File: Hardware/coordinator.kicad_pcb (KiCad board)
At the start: 4 copper layers, 140 x 140 mm, 111 parts, among them CON1 Nucleo-144-zio, CON10 Home Sensor, CON11 Home Sensor, CON12 Home Sensor, CON13 Home Sensor, CON14 Emergency Stop, CON15 Expansion, CON16 +24V Power in, CON2 DB25 Main Motor Signal, CON3 DB25 Main Motor Signal, CON4 DB25 Main Motor Signal, CON5 DB25 Main Motor Signal, CON6 DB25 Main Motor Signal, CON7 DB25 Main Motor Signal, CON8 Home Sensor, CON9 Home Sensor, J1 E5V, J2 PA1, U1 AM26LV32xD, U10 TLP293-4, U11 TLP293-4, U12 TLP293-4, U13 TLP293-4, U14 TLP293-4, U15 TLP293-4, U16 PDQE10, U2 AM26LV32xD, U3 AM26LV32xD, U4 DS26LV31T, U5 DS26LV31T, U6 DS26LV31T, U7 TLP293-4, U8 TLP293-4, U9 TLP293-4

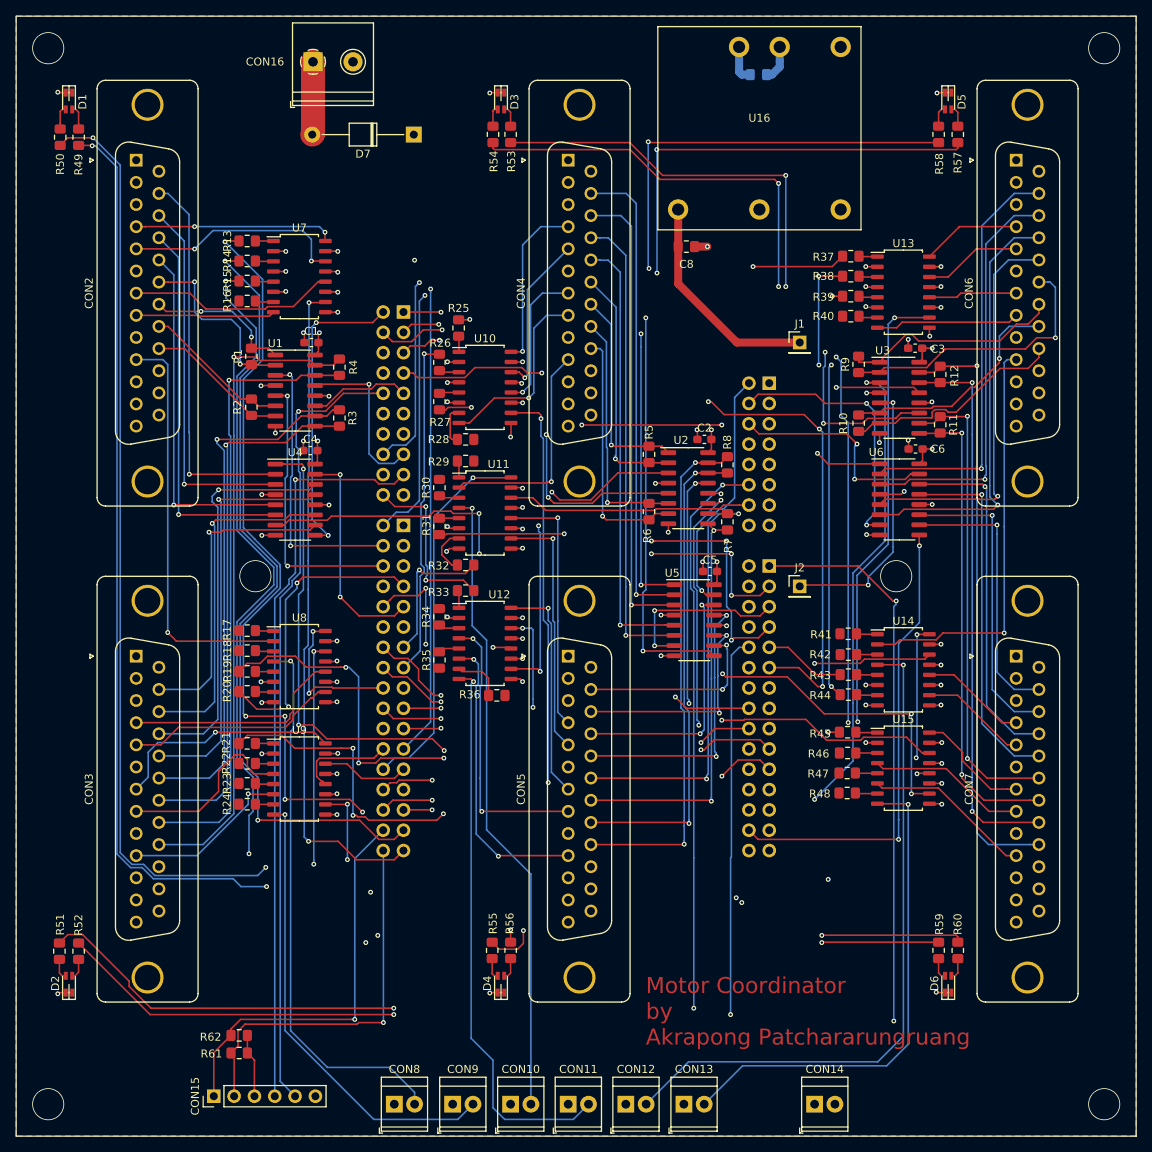
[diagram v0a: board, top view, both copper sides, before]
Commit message: Original commit of version 2. The firmware is similar to version 1 plus some bug fixes
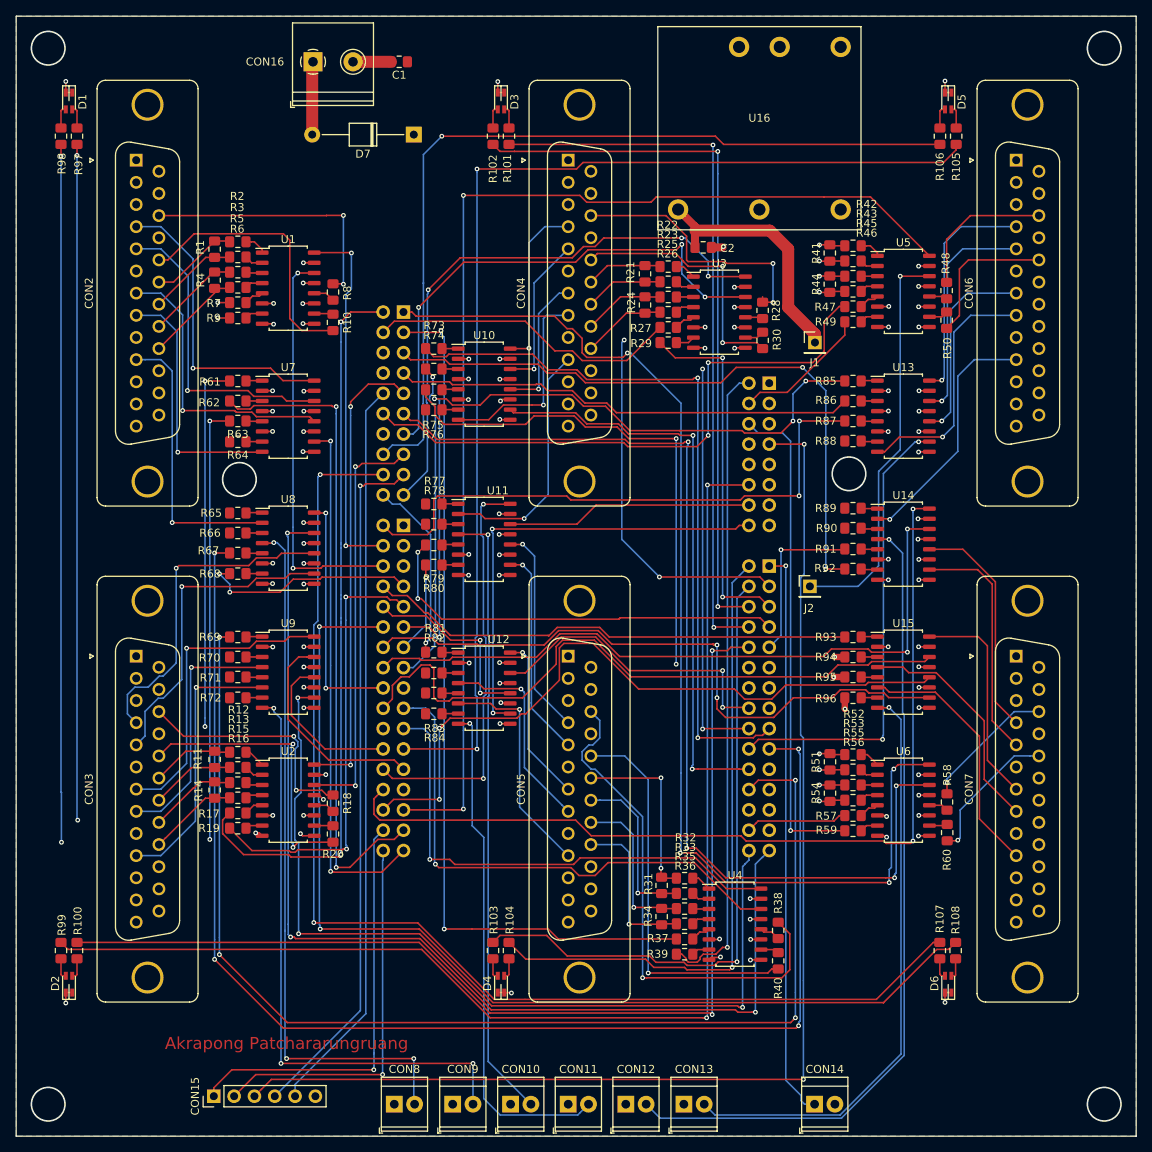
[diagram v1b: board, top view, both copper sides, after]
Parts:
- removed C3, C4, C5, C6: 0.1uF, Capacitor_SMD:C_0603_1608Metric_Pad1.05x0.95mm_HandSolder
- removed C7, C8: 10uF 25V, Capacitor_SMD:C_0805_2012Metric_Pad1.15x1.40mm_HandSolder
- added R100: 330, Resistor_SMD:R_0805_2012Metric_Pad1.15x1.40mm_HandSolder, F.Cu at (87.6, 136.8)
- added R101: 330, Resistor_SMD:R_0805_2012Metric_Pad1.15x1.40mm_HandSolder, F.Cu at (141.6, 35.0)
- added R102: 330, Resistor_SMD:R_0805_2012Metric_Pad1.15x1.40mm_HandSolder, F.Cu at (139.6, 35.0)
- added R103: 330, Resistor_SMD:R_0805_2012Metric_Pad1.15x1.40mm_HandSolder, F.Cu at (139.6, 136.8)
- added R104: 330, Resistor_SMD:R_0805_2012Metric_Pad1.15x1.40mm_HandSolder, F.Cu at (141.6, 136.8)
- added R105: 330, Resistor_SMD:R_0805_2012Metric_Pad1.15x1.40mm_HandSolder, F.Cu at (197.5, 35.0)
- added R106: 330, Resistor_SMD:R_0805_2012Metric_Pad1.15x1.40mm_HandSolder, F.Cu at (195.5, 35.0)
- added R107: 330, Resistor_SMD:R_0805_2012Metric_Pad1.15x1.40mm_HandSolder, F.Cu at (195.4, 136.8)
- added R108: 330, Resistor_SMD:R_0805_2012Metric_Pad1.15x1.40mm_HandSolder, F.Cu at (197.4, 136.8)
- added R63: 330, Resistor_SMD:R_0805_2012Metric_Pad1.15x1.40mm_HandSolder, F.Cu at (107.7, 70.6)
- added R64: 4.7K, Resistor_SMD:R_0805_2012Metric_Pad1.15x1.40mm_HandSolder, F.Cu at (107.7, 73.2)
- added R65: 4.7K, Resistor_SMD:R_0805_2012Metric_Pad1.15x1.40mm_HandSolder, F.Cu at (107.7, 82.1)
- added R66: 4.7K, Resistor_SMD:R_0805_2012Metric_Pad1.15x1.40mm_HandSolder, F.Cu at (107.7, 84.6)
- added R67: 330, Resistor_SMD:R_0805_2012Metric_Pad1.15x1.40mm_HandSolder, F.Cu at (107.7, 87.1)
- added R68: 330, Resistor_SMD:R_0805_2012Metric_Pad1.15x1.40mm_HandSolder, F.Cu at (107.7, 89.7)
- added R69: 330, Resistor_SMD:R_0805_2012Metric_Pad1.15x1.40mm_HandSolder, F.Cu at (107.7, 97.6)
- added R70: 4.7K, Resistor_SMD:R_0805_2012Metric_Pad1.15x1.40mm_HandSolder, F.Cu at (107.7, 100.1)
- added R71: 4.7K, Resistor_SMD:R_0805_2012Metric_Pad1.15x1.40mm_HandSolder, F.Cu at (107.7, 102.6)
- added R72: 4.7K, Resistor_SMD:R_0805_2012Metric_Pad1.15x1.40mm_HandSolder, F.Cu at (107.7, 105.2)
- added R73: 330, Resistor_SMD:R_0805_2012Metric_Pad1.15x1.40mm_HandSolder, F.Cu at (132.2, 61.5)
- added R74: 330, Resistor_SMD:R_0805_2012Metric_Pad1.15x1.40mm_HandSolder, F.Cu at (132.2, 64.1)
- added R75: 330, Resistor_SMD:R_0805_2012Metric_Pad1.15x1.40mm_HandSolder, F.Cu at (132.2, 66.7)
- added R76: 4.7K, Resistor_SMD:R_0805_2012Metric_Pad1.15x1.40mm_HandSolder, F.Cu at (132.2, 69.2)
- added R77: 4.7K, Resistor_SMD:R_0805_2012Metric_Pad1.15x1.40mm_HandSolder, F.Cu at (132.2, 81.0)
- added R78: 4.7K, Resistor_SMD:R_0805_2012Metric_Pad1.15x1.40mm_HandSolder, F.Cu at (132.2, 83.5)
- added R79: 330, Resistor_SMD:R_0805_2012Metric_Pad1.15x1.40mm_HandSolder, F.Cu at (132.2, 86.1)
- added R80: 330, Resistor_SMD:R_0805_2012Metric_Pad1.15x1.40mm_HandSolder, F.Cu at (132.2, 88.6)
- added R81: 330, Resistor_SMD:R_0805_2012Metric_Pad1.15x1.40mm_HandSolder, F.Cu at (132.2, 99.5)
- added R82: 4.7K, Resistor_SMD:R_0805_2012Metric_Pad1.15x1.40mm_HandSolder, F.Cu at (132.2, 102.1)
- added R83: 4.7K, Resistor_SMD:R_0805_2012Metric_Pad1.15x1.40mm_HandSolder, F.Cu at (132.2, 104.6)
- added R84: 4.7K, Resistor_SMD:R_0805_2012Metric_Pad1.15x1.40mm_HandSolder, F.Cu at (132.2, 107.2)
- added R85: 330, Resistor_SMD:R_0805_2012Metric_Pad1.15x1.40mm_HandSolder, F.Cu at (184.6, 65.6)
- added R86: 330, Resistor_SMD:R_0805_2012Metric_Pad1.15x1.40mm_HandSolder, F.Cu at (184.6, 68.1)
- added R87: 330, Resistor_SMD:R_0805_2012Metric_Pad1.15x1.40mm_HandSolder, F.Cu at (184.6, 70.6)
- added R88: 4.7K, Resistor_SMD:R_0805_2012Metric_Pad1.15x1.40mm_HandSolder, F.Cu at (184.6, 73.1)
- added R89: 4.7K, Resistor_SMD:R_0805_2012Metric_Pad1.15x1.40mm_HandSolder, F.Cu at (184.6, 81.5)
- added R90: 4.7K, Resistor_SMD:R_0805_2012Metric_Pad1.15x1.40mm_HandSolder, F.Cu at (184.6, 84.0)
- added R91: 330, Resistor_SMD:R_0805_2012Metric_Pad1.15x1.40mm_HandSolder, F.Cu at (184.6, 86.6)
- added R92: 330, Resistor_SMD:R_0805_2012Metric_Pad1.15x1.40mm_HandSolder, F.Cu at (184.6, 89.1)
- added R93: 330, Resistor_SMD:R_0805_2012Metric_Pad1.15x1.40mm_HandSolder, F.Cu at (184.6, 97.6)
- added R94: 4.7K, Resistor_SMD:R_0805_2012Metric_Pad1.15x1.40mm_HandSolder, F.Cu at (184.6, 100.1)
- added R95: 4.7K, Resistor_SMD:R_0805_2012Metric_Pad1.15x1.40mm_HandSolder, F.Cu at (184.6, 102.6)
- added R96: 4.7K, Resistor_SMD:R_0805_2012Metric_Pad1.15x1.40mm_HandSolder, F.Cu at (184.6, 105.2)
- added R97: 330, Resistor_SMD:R_0805_2012Metric_Pad1.15x1.40mm_HandSolder, F.Cu at (87.6, 35.0)
- added R98: 330, Resistor_SMD:R_0805_2012Metric_Pad1.15x1.40mm_HandSolder, F.Cu at (85.6, 35.0)
- added R99: 330, Resistor_SMD:R_0805_2012Metric_Pad1.15x1.40mm_HandSolder, F.Cu at (85.6, 136.8)
- C1, C2: value 0.1uF -> 10uF 25V; footprint Capacitor_SMD:C_0603_1608Metric_Pad1.05x0.95mm_HandSolder -> Capacitor_SMD:C_0805_2012Metric_Pad1.15x1.40mm_HandSolder
- R1, R11: value 120 -> 680
- R10, R8: value 120 -> 3.6k
- R12, R2, R3, R5, R6, R7, R9: value 120 -> 330
- R14, R44, R54: value 330 -> 120
- R16, R17, R22, R23, R29, R35, R36, R42, R46, R47, R61, R62: value 4.7K -> 330
- R18, R28, R30, R40, R48: value 4.7K -> 3.6k
- R20, R38, R50, R58, R60: value 330 -> 3.6k
- R21, R31, R51: value 330 -> 680
- R24, R34: value 4.7K -> 120
- R41: value 4.7K -> 680
- U1, U2, U3: value AM26LV32xD -> TLP292-4; footprint Package_SO:SOIC-16_3.9x9.9mm_P1.27mm -> Package_SO:SOIC-16_4.55x10.3mm_P1.27mm
- U10, U11, U12, U13, U14, U15, U7, U8, U9: value TLP293-4 -> TLP292-4
- U4, U5, U6: value DS26LV31T -> TLP292-4; footprint Package_SO:SOIC-16_3.9x9.9mm_P1.27mm -> Package_SO:SOIC-16_4.55x10.3mm_P1.27mm
- moved R50 113.1 mm to (196.3, 58.0), turned to 270 degrees
- moved R11 99.9 mm to (104.8, 112.9)
- moved R52 99.9 mm to (184.6, 112.3), turned to 0 degrees
- moved R12 99.7 mm to (107.7, 112.0), turned to 0 degrees
- moved R49 99.5 mm to (184.6, 58.2), turned to 0 degrees
- moved R51 99.2 mm to (181.7, 113.2)
- moved R54 92.5 mm to (181.7, 117.1), turned to 270 degrees
- moved R53 90.2 mm to (184.6, 114.2), turned to 0 degrees
- moved R37 87.8 mm to (163.6, 135.3), turned to 0 degrees
- moved R57 86.2 mm to (184.6, 119.9), turned to 0 degrees
- moved R39 84.8 mm to (163.6, 137.2), turned to 0 degrees
- moved R61 84.0 mm to (107.7, 65.6)
- moved R58 83.5 mm to (196.3, 118.2)
- moved R38 82.3 mm to (175.2, 134.3), turned to 90 degrees
- moved R23 81.9 mm to (161.5, 53.2), turned to 0 degrees
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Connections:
- C1 pad 1: GND -> +24V
- C1 pad 2: +3V3 -> GNDPWR
- C2 pad 1: GND -> +5V
- C2 pad 2: +3V3 -> GND
- CON2 pad 15: M1_PULSE_P -> +24V
- CON2 pad 17: M1_DIR_P -> +24V
- CON3 pad 15: M2_PULSE_P -> +24V
- CON3 pad 17: M2_DIR_P -> +24V
- CON4 pad 15: M3_PULSE_P -> +24V
- CON4 pad 17: M3_DIR_P -> +24V
- CON5 pad 15: M4_PULSE_P -> +24V
- CON5 pad 17: M4_DIR_P -> +24V
- CON6 pad 15: M5_PULSE_P -> +24V
- CON6 pad 17: M5_DIR_P -> +24V
- CON7 pad 15: M6_PULSE_P -> +24V
- CON7 pad 17: M6_DIR_P -> +24V
- R10 pad 1: M5_OUTB_P -> Net-(R10-Pad1)
- R10 pad 2: M5_OUTB_N -> M1_DIR_N
- R11 pad 1: M6_OUTA_P -> M2_OUTA_P
- R11 pad 2: M6_OUTA_N -> M2_OUTA_N
- R12 pad 1: M6_OUTB_P -> M2_OUTA_P
- R12 pad 2: M6_OUTB_N -> Net-(R12-Pad2)
- R13 pad 1: Net-(R13-Pad1) -> M2_OUTA_N
- R13 pad 2: M1_SRV_ON -> Net-(R13-Pad2)
- R14 pad 1: Net-(R14-Pad1) -> M2_OUTB_P
- R14 pad 2: M1_ALRM_RES -> M2_OUTB_N
- R15 pad 1: Net-(R15-Pad1) -> M2_OUTB_P
- R15 pad 2: M1_DEV_CLR -> Net-(R15-Pad2)
- R16 pad 1: Net-(R16-Pad1) -> M2_OUTB_N
- R16 pad 2: +24V -> Net-(R16-Pad2)
- R17 pad 1: Net-(R17-Pad1) -> M2_PULSE
- R17 pad 2: +24V -> Net-(R17-Pad2)
- R18 pad 2: +24V -> M2_PULSE_N
- R19 pad 1: Net-(R19-Pad1) -> M2_DIR
- R19 pad 2: M2_SRV_ON -> Net-(R19-Pad2)
- R2 pad 1: M1_OUTB_P -> M1_OUTA_P
- R2 pad 2: M1_OUTB_N -> Net-(R2-Pad2)
- R20 pad 2: M2_ALRM_RES -> M2_DIR_N
- R21 pad 1: Net-(R21-Pad1) -> M3_OUTA_P
- R21 pad 2: M2_DEV_CLR -> M3_OUTA_N
- R22 pad 1: Net-(R22-Pad1) -> M3_OUTA_P
- R22 pad 2: +24V -> Net-(R22-Pad2)
- R23 pad 1: Net-(R23-Pad1) -> M3_OUTA_N
- R23 pad 2: +24V -> Net-(R23-Pad2)
- R24 pad 1: Net-(R24-Pad1) -> M3_OUTB_P
- R24 pad 2: +24V -> M3_OUTB_N
- R25 pad 1: Net-(R25-Pad1) -> M3_OUTB_P
- R25 pad 2: M3_SRV_ON -> Net-(R25-Pad2)
- R26 pad 1: Net-(R26-Pad1) -> M3_OUTB_N
- R26 pad 2: M3_ALRM_RES -> Net-(R26-Pad2)
- R27 pad 1: Net-(R27-Pad1) -> M3_PULSE
- R27 pad 2: M3_DEV_CLR -> Net-(R27-Pad2)
- R28 pad 2: +24V -> M3_PULSE_N
- R29 pad 1: Net-(R29-Pad1) -> M3_DIR
- R29 pad 2: +24V -> Net-(R29-Pad2)
- R3 pad 1: M2_OUTA_P -> M1_OUTA_N
- R3 pad 2: M2_OUTA_N -> Net-(R3-Pad2)
- R30 pad 2: +24V -> M3_DIR_N
- R31 pad 1: Net-(R31-Pad1) -> M4_OUTA_P
- R31 pad 2: M4_SRV_ON -> M4_OUTA_N
- R32 pad 1: Net-(R32-Pad1) -> M4_OUTA_P
- R32 pad 2: M4_ALRM_RES -> Net-(R32-Pad2)
- R33 pad 1: Net-(R33-Pad1) -> M4_OUTA_N
- R33 pad 2: M4_DEV_CLR -> Net-(R33-Pad2)
- R34 pad 1: Net-(R34-Pad1) -> M4_OUTB_P
- R34 pad 2: +24V -> M4_OUTB_N
- R35 pad 1: Net-(R35-Pad1) -> M4_OUTB_P
- R35 pad 2: +24V -> Net-(R35-Pad2)
- R36 pad 1: Net-(R36-Pad1) -> M4_OUTB_N
- R36 pad 2: +24V -> Net-(R36-Pad2)
- R37 pad 1: Net-(R37-Pad1) -> M4_PULSE
- R37 pad 2: M5_SRV_ON -> Net-(R37-Pad2)
- R38 pad 2: M5_ALRM_RES -> M4_PULSE_N
- R39 pad 1: Net-(R39-Pad1) -> M4_DIR
- R39 pad 2: M5_DEV_CLR -> Net-(R39-Pad2)
- R4 pad 1: M2_OUTB_P -> M1_OUTB_P
- R4 pad 2: M2_OUTB_N -> M1_OUTB_N
- R40 pad 2: +24V -> M4_DIR_N
- R41 pad 1: Net-(R41-Pad1) -> M5_OUTA_P
- R41 pad 2: +24V -> M5_OUTA_N
- R42 pad 1: Net-(R42-Pad1) -> M5_OUTA_P
- R42 pad 2: +24V -> Net-(R42-Pad2)
- R43 pad 1: Net-(R43-Pad1) -> M5_OUTA_N
- R43 pad 2: M6_SRV_ON -> Net-(R43-Pad2)
- R44 pad 1: Net-(R44-Pad1) -> M5_OUTB_P
- R44 pad 2: M6_ALRM_RES -> M5_OUTB_N
- R45 pad 1: Net-(R45-Pad1) -> M5_OUTB_P
- R45 pad 2: M6_DEV_CLR -> Net-(R45-Pad2)
- R46 pad 1: Net-(R46-Pad1) -> M5_OUTB_N
- R46 pad 2: +24V -> Net-(R46-Pad2)
- R47 pad 1: Net-(R47-Pad1) -> M5_PULSE
- R47 pad 2: +24V -> Net-(R47-Pad2)
- R48 pad 2: +24V -> M5_PULSE_N
- R49 pad 1: Net-(CON1-Pad9-25) -> M5_DIR
- R49 pad 2: Net-(D1-Pad2) -> Net-(R49-Pad2)
- R5 pad 1: M3_OUTA_P -> M1_OUTB_P
- R5 pad 2: M3_OUTA_N -> Net-(R5-Pad2)
- R50 pad 1: Net-(CON1-Pad9-27) -> Net-(R50-Pad1)
- R50 pad 2: Net-(D1-Pad4) -> M5_DIR_N
- R51 pad 1: Net-(CON1-Pad8-12) -> M6_OUTA_P
- R51 pad 2: Net-(D2-Pad2) -> M6_OUTA_N
- R52 pad 1: Net-(CON1-Pad9-10) -> M6_OUTA_P
- R52 pad 2: Net-(D2-Pad4) -> Net-(R52-Pad2)
- R53 pad 1: Net-(CON1-Pad9-8) -> M6_OUTA_N
- R53 pad 2: Net-(D3-Pad2) -> Net-(R53-Pad2)
- R54 pad 1: Net-(CON1-Pad9-6) -> M6_OUTB_P
- R54 pad 2: Net-(D3-Pad4) -> M6_OUTB_N
- R55 pad 1: Net-(CON1-Pad9-4) -> M6_OUTB_P
- R55 pad 2: Net-(D4-Pad2) -> Net-(R55-Pad2)
- R56 pad 1: Net-(CON1-Pad9-2) -> M6_OUTB_N
- R56 pad 2: Net-(D4-Pad4) -> Net-(R56-Pad2)
- R57 pad 1: Net-(CON1-Pad10-23) -> M6_PULSE
- R57 pad 2: Net-(D5-Pad2) -> Net-(R57-Pad2)
- R58 pad 1: Net-(CON1-Pad7-16) -> Net-(R58-Pad1)
- R58 pad 2: Net-(D5-Pad4) -> M6_PULSE_N
- R59 pad 1: Net-(CON1-Pad7-18) -> M6_DIR
- R59 pad 2: Net-(D6-Pad2) -> Net-(R59-Pad2)
- R6 pad 1: M3_OUTB_P -> M1_OUTB_N
- R6 pad 2: M3_OUTB_N -> Net-(R6-Pad2)
- R60 pad 1: Net-(CON1-Pad10-12) -> Net-(R60-Pad1)
- R60 pad 2: Net-(D6-Pad4) -> M6_DIR_N
- R61 pad 1: +3V3 -> Net-(R61-Pad1)
- R61 pad 2: I2C_SDA -> M1_SRV_ON
- R62 pad 1: +3V3 -> Net-(R62-Pad1)
- R62 pad 2: I2C_SCL -> M1_ALRM_RES
- R7 pad 1: M4_OUTA_P -> M1_PULSE
- R7 pad 2: M4_OUTA_N -> Net-(R7-Pad2)
- R8 pad 1: M4_OUTB_P -> Net-(R8-Pad1)
- R8 pad 2: M4_OUTB_N -> M1_PULSE_N
- R9 pad 1: M5_OUTA_P -> M1_DIR
- R9 pad 2: M5_OUTA_N -> Net-(R9-Pad2)
- U1 pad 1: M1_OUTA_N -> Net-(R2-Pad2)
- U1 pad 10: M2_OUTA_P -> Net-(R10-Pad1)
- U1 pad 11: M2_ENCA -> GNDPWR
- U1 pad 12: GND -> Net-(R8-Pad1)
- U1 pad 13: M2_ENCB -> GND
- U1 pad 14: M2_OUTB_P -> M1_ENCB
- U1 pad 15: M2_OUTB_N -> GND
- U1 pad 16: +3V3 -> M1_ENCA
- U1 pad 2: M1_OUTA_P -> Net-(R3-Pad2)
- U1 pad 3: M1_ENCA -> Net-(R5-Pad2)
- U1 pad 4: +3V3 -> Net-(R6-Pad2)
- U1 pad 5: M1_ENCB -> Net-(R7-Pad2)
- U1 pad 6: M1_OUTB_P -> GND
- U1 pad 7: M1_OUTB_N -> Net-(R9-Pad2)
- U1 pad 9: M2_OUTA_N -> GNDPWR
- U10 pad 1: Net-(R25-Pad1) -> Net-(R73-Pad1)
- U10 pad 3: Net-(R26-Pad1) -> Net-(R74-Pad1)
- U10 pad 5: Net-(R27-Pad1) -> Net-(R75-Pad1)
- U10 pad 7: Net-(R28-Pad1) -> Net-(R76-Pad1)
- U11 pad 1: Net-(R29-Pad1) -> Net-(R77-Pad1)
- U11 pad 3: Net-(R30-Pad1) -> Net-(R78-Pad1)
- U11 pad 5: Net-(R31-Pad1) -> Net-(R79-Pad1)
- U11 pad 7: Net-(R32-Pad1) -> Net-(R80-Pad1)
- U12 pad 1: Net-(R33-Pad1) -> Net-(R81-Pad1)
- U12 pad 3: Net-(R34-Pad1) -> Net-(R82-Pad1)
- U12 pad 5: Net-(R35-Pad1) -> Net-(R83-Pad1)
- U12 pad 7: Net-(R36-Pad1) -> Net-(R84-Pad1)
- U13 pad 1: Net-(R37-Pad1) -> Net-(R85-Pad1)
- U13 pad 3: Net-(R38-Pad1) -> Net-(R86-Pad1)
- U13 pad 5: Net-(R39-Pad1) -> Net-(R87-Pad1)
- U13 pad 7: Net-(R40-Pad1) -> Net-(R88-Pad1)
- U14 pad 1: Net-(R41-Pad1) -> Net-(R89-Pad1)
- U14 pad 3: Net-(R42-Pad1) -> Net-(R90-Pad1)
- U14 pad 5: Net-(R43-Pad1) -> Net-(R91-Pad1)
- U14 pad 7: Net-(R44-Pad1) -> Net-(R92-Pad1)
- U15 pad 1: Net-(R45-Pad1) -> Net-(R93-Pad1)
- U15 pad 3: Net-(R46-Pad1) -> Net-(R94-Pad1)
- U15 pad 5: Net-(R47-Pad1) -> Net-(R95-Pad1)
- U15 pad 7: Net-(R48-Pad1) -> Net-(R96-Pad1)
- U2 pad 1: M3_OUTA_N -> Net-(R12-Pad2)
- U2 pad 10: M4_OUTA_P -> Net-(R20-Pad1)
- U2 pad 11: M4_ENCA -> GNDPWR
- U2 pad 12: GND -> Net-(R18-Pad1)
- U2 pad 13: M4_ENCB -> GND
- U2 pad 14: M4_OUTB_P -> M2_ENCB
- U2 pad 15: M4_OUTB_N -> GND
- U2 pad 16: +3V3 -> M2_ENCA
- U2 pad 2: M3_OUTA_P -> Net-(R13-Pad2)
- U2 pad 3: M3_ENCA -> Net-(R15-Pad2)
- U2 pad 4: +3V3 -> Net-(R16-Pad2)
- U2 pad 5: M3_ENCB -> Net-(R17-Pad2)
- U2 pad 6: M3_OUTB_P -> GND
- U2 pad 7: M3_OUTB_N -> Net-(R19-Pad2)
- U2 pad 9: M4_OUTA_N -> GNDPWR
- U3 pad 1: M5_OUTA_N -> Net-(R22-Pad2)
- U3 pad 10: M6_OUTA_P -> Net-(R30-Pad1)
- U3 pad 11: M6_ENCA -> GNDPWR
- U3 pad 12: GND -> Net-(R28-Pad1)
- U3 pad 13: M6_ENCB -> GND
- U3 pad 14: M6_OUTB_P -> M3_ENCB
- U3 pad 15: M6_OUTB_N -> GND
- U3 pad 16: +3V3 -> M3_ENCA
- U3 pad 2: M5_OUTA_P -> Net-(R23-Pad2)
- U3 pad 3: M5_ENCA -> Net-(R25-Pad2)
- U3 pad 4: +3V3 -> Net-(R26-Pad2)
- U3 pad 5: M5_ENCB -> Net-(R27-Pad2)
- U3 pad 6: M5_OUTB_P -> GND
- U3 pad 7: M5_OUTB_N -> Net-(R29-Pad2)
- U3 pad 9: M6_OUTA_N -> GNDPWR
- U4 pad 1: M1_PULSE -> Net-(R32-Pad2)
- U4 pad 10: M2_PULSE_P -> Net-(R40-Pad1)
- U4 pad 11: M2_PULSE_N -> GNDPWR
- U4 pad 12: GND -> Net-(R38-Pad1)
- U4 pad 13: M2_DIR_N -> GND
- U4 pad 14: M2_DIR_P -> M4_ENCB
- U4 pad 15: M2_DIR -> GND
- U4 pad 16: +3V3 -> M4_ENCA
- U4 pad 2: M1_PULSE_P -> Net-(R33-Pad2)
- U4 pad 3: M1_PULSE_N -> Net-(R35-Pad2)
- U4 pad 4: +3V3 -> Net-(R36-Pad2)
- U4 pad 5: M1_DIR_N -> Net-(R37-Pad2)
- U4 pad 6: M1_DIR_P -> GND
- U4 pad 7: M1_DIR -> Net-(R39-Pad2)
- U4 pad 9: M2_PULSE -> GNDPWR
- U5 pad 1: M3_PULSE -> Net-(R42-Pad2)
- U5 pad 10: M4_PULSE_P -> Net-(R50-Pad1)
- U5 pad 11: M4_PULSE_N -> GNDPWR
- U5 pad 12: GND -> Net-(R48-Pad1)
- U5 pad 13: M4_DIR_N -> GND
- U5 pad 14: M4_DIR_P -> M5_ENCB
- U5 pad 15: M4_DIR -> GND
- U5 pad 16: +3V3 -> M5_ENCA
- U5 pad 2: M3_PULSE_P -> Net-(R43-Pad2)
- U5 pad 3: M3_PULSE_N -> Net-(R45-Pad2)
- U5 pad 4: +3V3 -> Net-(R46-Pad2)
- U5 pad 5: M3_DIR_N -> Net-(R47-Pad2)
- U5 pad 6: M3_DIR_P -> GND
- U5 pad 7: M3_DIR -> Net-(R49-Pad2)
- U5 pad 9: M4_PULSE -> GNDPWR
- U6 pad 1: M5_PULSE -> Net-(R52-Pad2)
- U6 pad 10: M6_PULSE_P -> Net-(R60-Pad1)
- U6 pad 11: M6_PULSE_N -> GNDPWR
- U6 pad 12: GND -> Net-(R58-Pad1)
- U6 pad 13: M6_DIR_N -> GND
- U6 pad 14: M6_DIR_P -> M6_ENCB
- U6 pad 15: M6_DIR -> GND
- U6 pad 16: +3V3 -> M6_ENCA
- U6 pad 2: M5_PULSE_P -> Net-(R53-Pad2)
- U6 pad 3: M5_PULSE_N -> Net-(R55-Pad2)
- U6 pad 4: +3V3 -> Net-(R56-Pad2)
- U6 pad 5: M5_DIR_N -> Net-(R57-Pad2)
- U6 pad 6: M5_DIR_P -> GND
- U6 pad 7: M5_DIR -> Net-(R59-Pad2)
- U6 pad 9: M6_PULSE -> GNDPWR
- U7 pad 1: Net-(R13-Pad1) -> Net-(R61-Pad1)
- U7 pad 3: Net-(R14-Pad1) -> Net-(R62-Pad1)
- U7 pad 5: Net-(R15-Pad1) -> Net-(R63-Pad1)
- U7 pad 7: Net-(R16-Pad1) -> Net-(R64-Pad1)
- U8 pad 1: Net-(R17-Pad1) -> Net-(R65-Pad1)
- U8 pad 3: Net-(R18-Pad1) -> Net-(R66-Pad1)
- U8 pad 5: Net-(R19-Pad1) -> Net-(R67-Pad1)
- U8 pad 7: Net-(R20-Pad1) -> Net-(R68-Pad1)
- U9 pad 1: Net-(R21-Pad1) -> Net-(R69-Pad1)
- U9 pad 3: Net-(R22-Pad1) -> Net-(R70-Pad1)
- U9 pad 5: Net-(R23-Pad1) -> Net-(R71-Pad1)
- U9 pad 7: Net-(R24-Pad1) -> Net-(R72-Pad1)
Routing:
- net +3V3: track 38.2 -> 153.6 mm, vias 12 -> 2
- net M2_SRV_ON: track 80.8 -> 167.8 mm
- net M2_DEV_CLR: track 75.8 -> 152.7 mm, vias 3 -> 4
- net M2_OUTB_N: track 82.1 -> 11.3 mm, vias 1 -> 0
- net M2_OUTB_P: track 77.5 -> 11.0 mm, vias 1 -> 0
- net M6_ENCA: track 78.3 -> 144.0 mm, vias 3 -> 4
- net M6_ENCB: track 68.5 -> 131.4 mm, vias 1 -> 4
- net M3_PULSE_P: track 59.9 -> 0.00 mm, vias 1 -> 0
- net M3_DIR_P: track 58.9 -> 0.00 mm, vias 1 -> 0
- net M2_OUTA_N: track 67.4 -> 10.5 mm, vias 1 -> 0
- net M2_OUTA_P: track 66.6 -> 10.3 mm, vias 1 -> 0
- net M6_DEV_CLR: track 117.2 -> 61.2 mm, vias 3 -> 0
- net M5_DIR_P: track 53.4 -> 0.00 mm, vias 1 -> 0
- net M2_PULSE: track 38.2 -> 91.5 mm
- net M5_PULSE_P: track 52.2 -> 0.00 mm, vias 1 -> 0
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- added copper zone on B.Cu, net +24V
- removed copper zone on B.Cu, net +3V3
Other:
- board text added: "Akrapong Patchararungruang"
- board text removed: "Motor Coordinator by Akrapong Patchararungruang"

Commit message: Version 2.0.1. Fixed Home-sensor connection bug
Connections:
- CON10 pad 1: +24V -> GNDPWR
- CON11 pad 1: +24V -> GNDPWR
- CON12 pad 1: +24V -> GNDPWR
- CON13 pad 1: +24V -> GNDPWR
- CON8 pad 1: +24V -> GNDPWR
- CON9 pad 1: +24V -> GNDPWR
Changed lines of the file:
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@@
       (net 196 M6_HOME_EXT))
     (pad 1 thru_hole rect (at 0 0) (size 2.1 2.1) (drill 1.1) (layers *.Cu *.Mask)
-      (net 4 +24V))
+      (net 3 GNDPWR))
     (model ${KISYS3DMOD}/TerminalBlock_TE-Connectivity.3dshapes/TerminalBlock_TE_282834-2_1x02_P2.54mm_Horizontal.wrl
       (at (xyz 0 0 0))
@@
       (net 195 M5_HOME_EXT))
     (pad 1 thru_hole rect (at 0 0) (size 2.1 2.1) (drill 1.1) (layers *.Cu *.Mask)
-      (net 4 +24V))
+      (net 3 GNDPWR))
     (model ${KISYS3DMOD}/TerminalBlock_TE-Connectivity.3dshapes/TerminalBlock_TE_282834-2_1x02_P2.54mm_Horizontal.wrl
       (at (xyz 0 0 0))
@@
       (net 194 M4_HOME_EXT))
     (pad 1 thru_hole rect (at 0 0) (size 2.1 2.1) (drill 1.1) (layers *.Cu *.Mask)
-      (net 4 +24V))
+      (net 3 GNDPWR))
     (model ${KISYS3DMOD}/TerminalBlock_TE-Connectivity.3dshapes/TerminalBlock_TE_282834-2_1x02_P2.54mm_Horizontal.wrl
       (at (xyz 0 0 0))
@@
       (net 193 M3_HOME_EXT))
     (pad 1 thru_hole rect (at 0 0) (size 2.1 2.1) (drill 1.1) (layers *.Cu *.Mask)
-      (net 4 +24V))
+      (net 3 GNDPWR))
     (model ${KISYS3DMOD}/TerminalBlock_TE-Connectivity.3dshapes/TerminalBlock_TE_282834-2_1x02_P2.54mm_Horizontal.wrl
       (at (xyz 0 0 0))
@@
       (net 192 M2_HOME_EXT))
     (pad 1 thru_hole rect (at 0 0) (size 2.1 2.1) (drill 1.1) (layers *.Cu *.Mask)
-      (net 4 +24V))
+      (net 3 GNDPWR))
     (model ${KISYS3DMOD}/TerminalBlock_TE-Connectivity.3dshapes/TerminalBlock_TE_282834-2_1x02_P2.54mm_Horizontal.wrl
       (at (xyz 0 0 0))
@@
       (net 191 M1_HOME_EXT))
     (pad 1 thru_hole rect (at 0 0) (size 2.1 2.1) (drill 1.1) (layers *.Cu *.Mask)
-      (net 4 +24V))
+      (net 3 GNDPWR))
     (model ${KISYS3DMOD}/TerminalBlock_TE-Connectivity.3dshapes/TerminalBlock_TE_282834-2_1x02_P2.54mm_Horizontal.wrl
       (at (xyz 0 0 0))
@@
   (gr_line (start 220 20) (end 220 160) (layer Edge.Cuts) (width 0.05))
   (gr_line (start 80 20) (end 220 20) (layer Edge.Cuts) (width 0.05))
+  (via (at 84 156) (size 4.4) (drill 4) (layers F.Cu B.Cu) (net 0))
+  (via (at 84 24) (size 4.4) (drill 4) (layers F.Cu B.Cu) (net 0))
+  (via (at 216 156) (size 4.4) (drill 4) (layers F.Cu B.Cu) (net 0))
+  (via (at 216 24) (size 4.4) (drill 4) (layers F.Cu B.Cu) (net 0))
+  (via (at 107.9 77.9) (size 4.4) (drill 4) (layers F.Cu B.Cu) (net 0))
+  (via (at 184.1 77.2) (size 4.4) (drill 4) (layers F.Cu B.Cu) (net 0))
   (via (at 178.5 73.5) (size 0.6) (drill 0.3) (layers F.Cu B.Cu) (net 1))
   (segment (start 178.49 73.49) (end 178.5 73.5) (width 0.2) (layer F.Cu) (net 1))
@@
   (segment (start 183.575 106.575) (end 183.6 106.6) (width 0.8) (layer F.Cu) (net 4))
   (segment (start 183.575 105.2) (end 183.575 106.575) (width 0.8) (layer F.Cu) (net 4))
-  (via (at 84 156) (size 4.4) (drill 4) (layers F.Cu B.Cu) (net 0))
-  (via (at 84 24) (size 4.4) (drill 4) (layers F.Cu B.Cu) (net 0))
-  (via (at 216 156) (size 4.4) (drill 4) (layers F.Cu B.Cu) (net 0))
-  (via (at 216 24) (size 4.4) (drill 4) (layers F.Cu B.Cu) (net 0))
-  (via (at 107.9 77.9) (size 4.4) (drill 4) (layers F.Cu B.Cu) (net 0))
-  (via (at 184.1 77.2) (size 4.4) (drill 4) (layers F.Cu B.Cu) (net 0))
   (segment (start 164.85 46.27) (end 162.74 44.16) (width 1) (layer F.Cu) (net 5))
   (segment (start 174.2 46.8) (end 164.9 46.8) (width 1.5) (layer F.Cu) (net 5))
